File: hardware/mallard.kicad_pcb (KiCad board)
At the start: 4 copper layers, 101.6 x 101.6 mm, 81 parts, among them J1 USB_A, J2 Conn_02x03_Odd_Even, J3 Conn_01x03, J4 Conn_01x03, J5 Conn_01x03, J6 Conn_01x03, SW1 RESET Switch, U10 LTC1983ES6-3, U11 STM32L4Q5xx, U12 LTC3529EDCB, U4 BQ24210DQCT, U5 TMUX1309, U6 TMUX1309, U7 LMP7721, U8 TPS71710DRVR, U9 LMV554

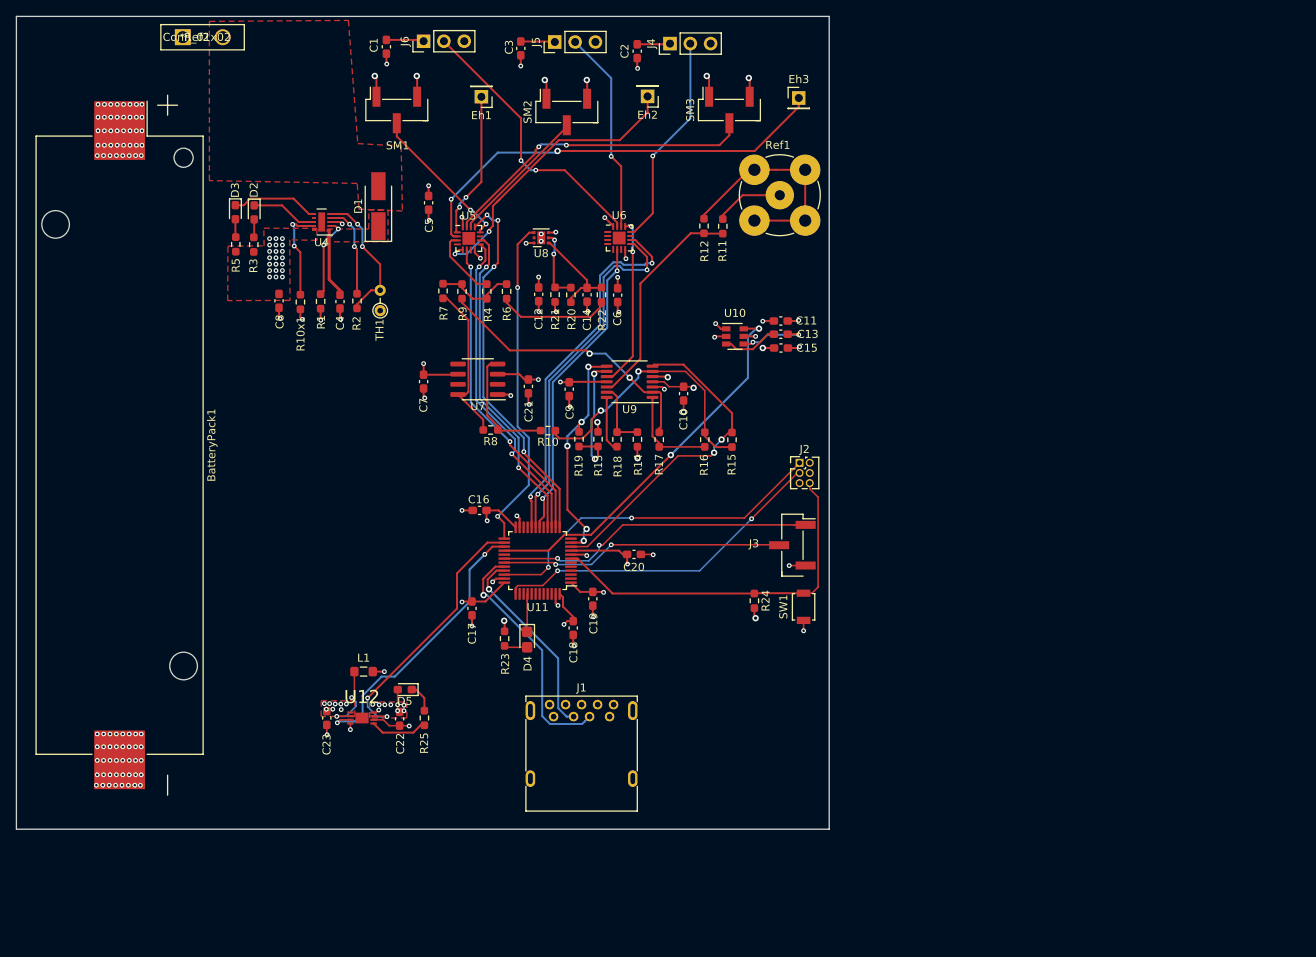
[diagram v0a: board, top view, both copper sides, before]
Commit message: Revised layout, fixed schematic errors
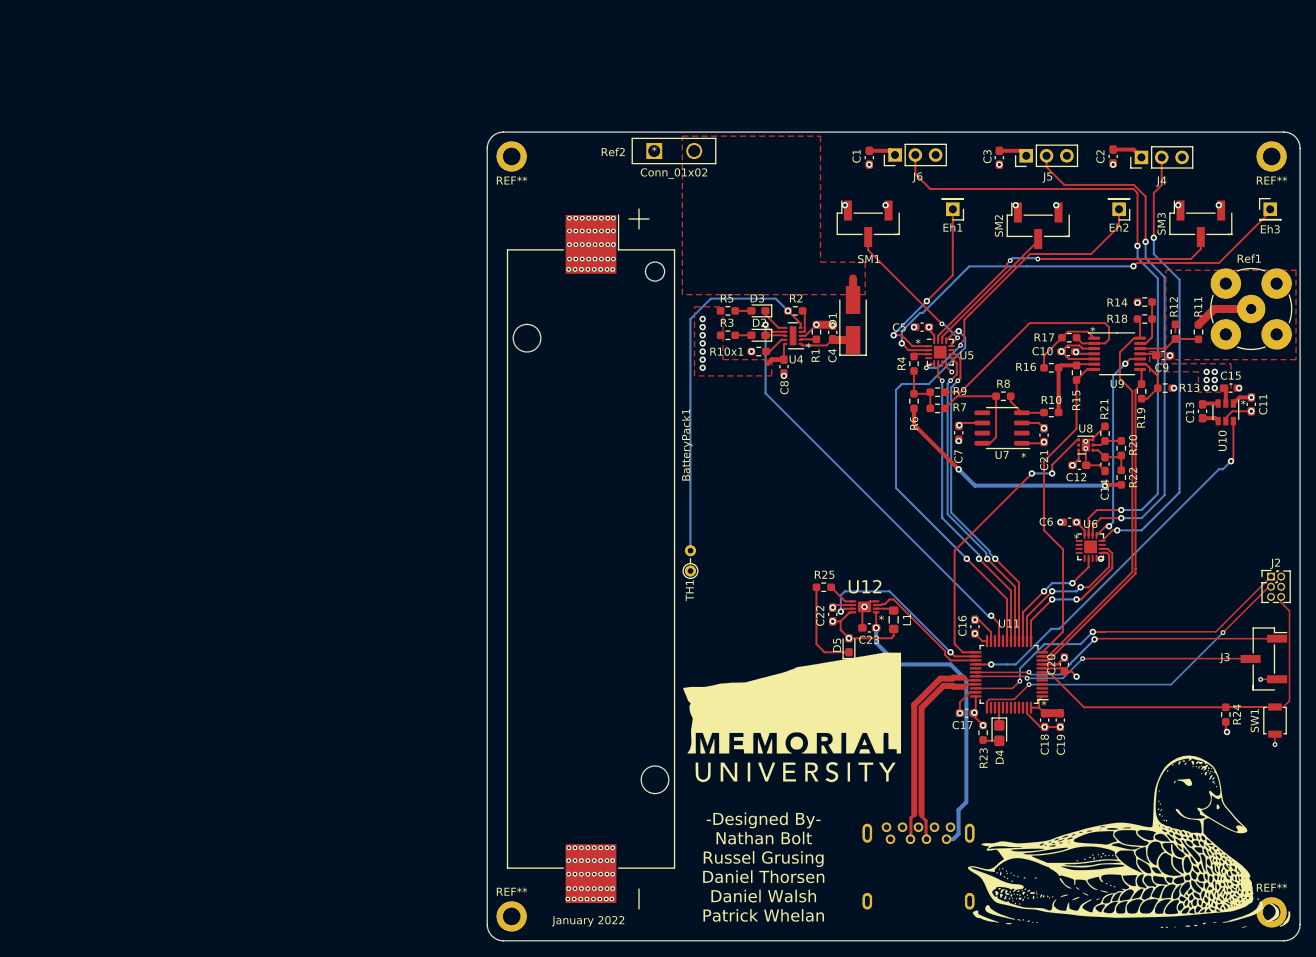
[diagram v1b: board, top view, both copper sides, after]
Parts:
- added G***: LOGO, hardware:mallardImage, F.Cu at (178.8, 136.7)
- added G***: LOGO, hardware:munLogo, F.Cu at (137.2, 121.4)
- added REF**: MountingHole_2.2mm_M2_DIN965_Pad, MountingHole:MountingHole_2.2mm_M2_DIN965_Pad, F.Cu at (197.1, 51.3)
- added REF**: MountingHole_2.2mm_M2_DIN965_Pad, MountingHole:MountingHole_2.2mm_M2_DIN965_Pad, F.Cu at (197.1, 145.8)
- added REF**: MountingHole_2.2mm_M2_DIN965_Pad, MountingHole:MountingHole_2.2mm_M2_DIN965_Pad, F.Cu at (102.1, 146.3)
- added REF**: MountingHole_2.2mm_M2_DIN965_Pad, MountingHole:MountingHole_2.2mm_M2_DIN965_Pad, F.Cu at (102.1, 51.3)
- J1: moved to B.Cu
- moved C9 74.4 mm to (183.5, 76.2), turned to 0 degrees
- moved U8 72.8 mm to (173.9, 87.4)
- moved R20 71.4 mm to (178.3, 87.8)
- moved R13 71.2 mm to (183.8, 80.3), turned to 180 degrees
- moved R21 70.9 mm to (176.3, 86.0), turned to 90 degrees
- moved C12 70.9 mm to (173.1, 89.9), turned to 0 degrees
- moved R19 70.6 mm to (180.8, 80.7)
- moved U6 70.4 mm to (174.5, 100.1)
- moved R22 68.9 mm to (178.3, 91.4)
- moved C23 68.7 mm to (146.8, 110.2), turned to 180 degrees
- moved C14 68.1 mm to (176.3, 89.8)
- moved R18 67.7 mm to (181.3, 71.6), turned to 0 degrees
- moved C7 67.2 mm to (158.0, 85.9)
- moved L1 66.6 mm to (149.9, 109.2), turned to 90 degrees
- moved D3 66.5 mm to (133.0, 70.6), turned to 180 degrees
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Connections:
- U11 pad 10: Eh_Sense -> Temp_Sense
- U11 pad 11: Temp_Sense -> Ref_Out
- U11 pad 12: Ref_Elec -> Eh_Sense
- U11 pad 13: Moisture_Sense -> MUX2_A1
- U11 pad 14: MUX1_EN -> MUX2_A0
- U11 pad 15: MUX1_A0 -> MUX2_EN
- U11 pad 17: Net-(U11-Pad17) -> MUX1_A0
- U11 pad 18: MUX2_EN -> MUX1_EN
- U11 pad 19: MUX2_A0 -> Moisture_Sense
- U11 pad 20: MUX2_A1 -> Net-(U11-Pad20)
- U12 pad 9: (no net) -> GND
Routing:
- net Charge_EN: track 0.00 -> 54.8 mm, vias 0 -> 2
- net Net-(J6-Pad2): track 34.6 -> 82.3 mm
- net Ref_Out: track 6.97 -> 49.5 mm
- net Net-(J5-Pad2): track 25.4 -> 65.4 mm, vias 1 -> 2
- net +5V: track 0.00 -> 38.4 mm, vias 8 -> 2
- net Net-(J4-Pad2): track 26.9 -> 55.8 mm, vias 1 -> 2
- net MUX2_A1: track 46.9 -> 18.8 mm
- net Net-(R2-Pad2): track 17.6 -> 45.6 mm, vias 2 -> 1
- net Net-(R12-Pad2): track 28.2 -> 1.16 mm
- net MUX2_A0: track 45.4 -> 18.8 mm
- net Net-(R10-Pad1): track 34.7 -> 10.2 mm, vias 2 -> 0
- net MUX2_EN: track 38.9 -> 15.2 mm
- net Net-(R11-Pad1): track 28.0 -> 7.83 mm
- net +3V3: track 80.3 -> 60.7 mm, vias 91 -> 63
- net 5V_SHDN_L: track 35.5 -> 16.1 mm, vias 2 -> 0
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- added copper zone on F.Cu, net -3V3
- added copper zone on F.Cu, net Net-(R12-Pad2)
- removed copper zone on F.Cu, net +5V
- removed copper zone on Power, net +5V
- removed copper zone on F.Cu, net Net-(C4-Pad1)
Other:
- board size 101.6 x 101.6 mm -> 101.6 x 101.1 mm
- board text added: "*"
- board text added: "-Designed By- Nathan Bolt Russel Grusing Daniel Thorsen Daniel Walsh Patrick Whelan"
- board text added: "January 2022"

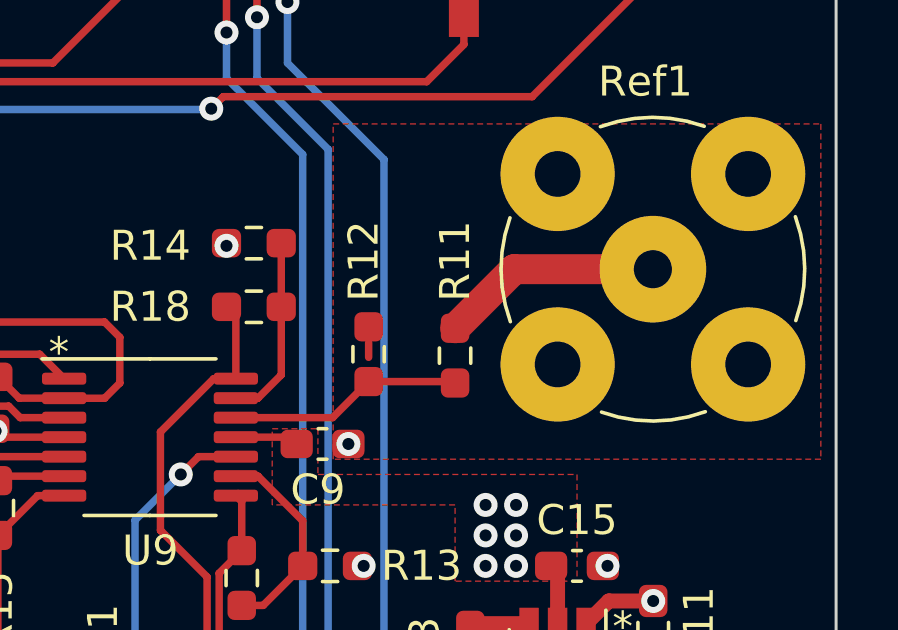
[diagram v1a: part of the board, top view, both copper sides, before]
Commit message: Changes some components on BOM
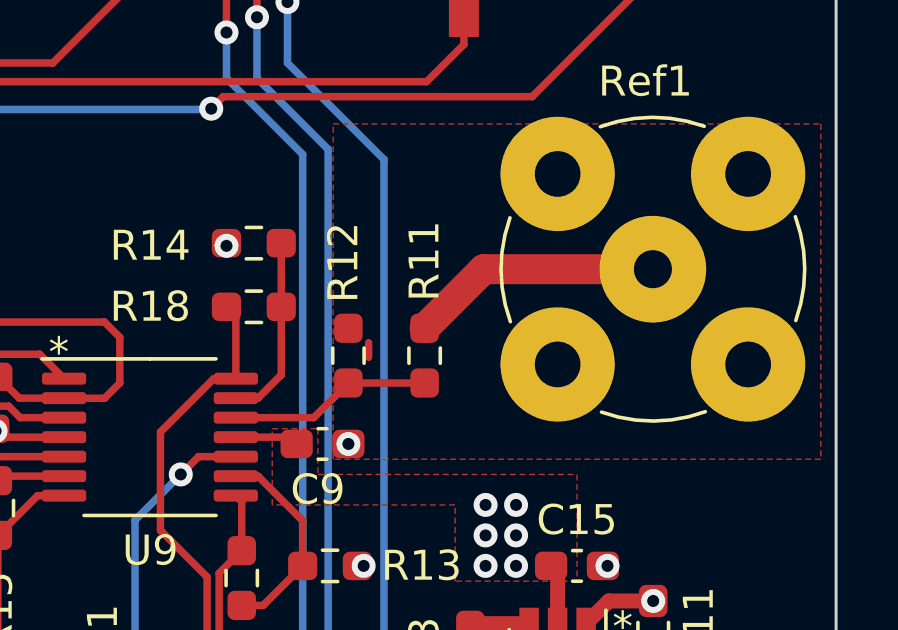
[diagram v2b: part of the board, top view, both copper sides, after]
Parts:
- moved R11 1.02 mm to (186.9, 73.3)
- moved R12 0.68 mm to (184.4, 73.3)
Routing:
- net Net-(R11-Pad1): track 7.83 -> 6.77 mm
- net Net-(R11-Pad2): track 7.41 -> 8.42 mm

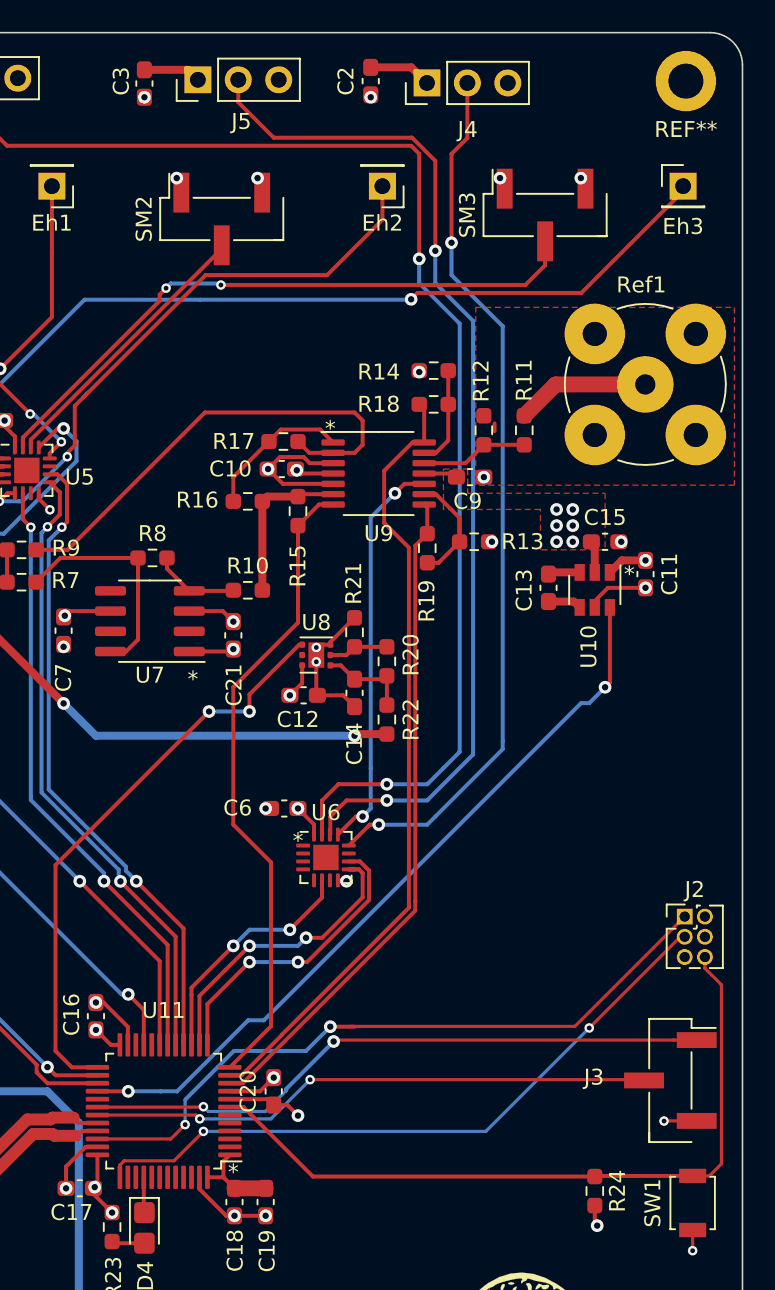
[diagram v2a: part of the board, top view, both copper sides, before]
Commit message: Replaced -3V charge pump with LM828
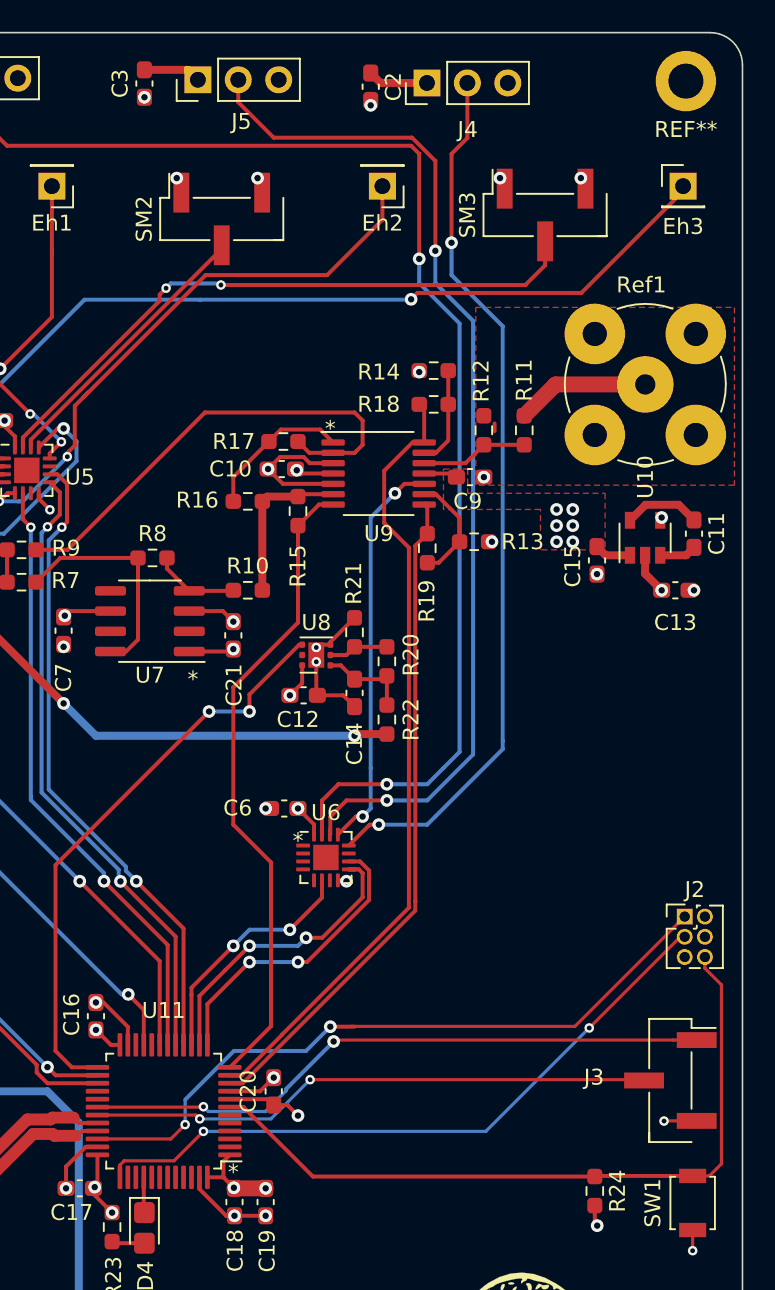
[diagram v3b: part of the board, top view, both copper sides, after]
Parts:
- C15: value 10uF -> 1uF
- U10: value LTC1983ES6-3 -> LM828; footprint Package_TO_SOT_SMD:SOT-23-6 -> Package_TO_SOT_SMD:SOT-23-5
- moved C13 7.98 mm to (196.4, 83.3), turned to 0 degrees
- moved U10 4.55 mm to (194.5, 80.0), turned to 90 degrees
- moved C11 3.97 mm to (197.6, 79.8)
- moved C15 1.28 mm to (191.5, 81.4), turned to 270 degrees
- moved C2 0.35 mm to (177.3, 51.7)
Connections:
- C11 pad 1: +3V3 -> Net-(C11-Pad1)
- C11 pad 2: GND -> Net-(C11-Pad2)
- C13 pad 1: Net-(C13-Pad1) -> +3V3
- C13 pad 2: Net-(C13-Pad2) -> GND
- U10 pad 1: +3V3 -> -3V3
- U10 pad 2: -3V3 -> +3V3
- U10 pad 3: Net-(C13-Pad1) -> Net-(C11-Pad2)
- U10 pad 4: Net-(C13-Pad2) -> GND
- U10 pad 5: GND -> Net-(C11-Pad1)
- U11 pad 28: -3V3_SHDN_L -> Net-(U11-Pad28)
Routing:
- net -3V3_SHDN_L: track 47.6 -> 0.00 mm, vias 2 -> 0
- net Net-(C11-Pad1): track 0.00 -> 4.82 mm
- net GND: track 58.8 -> 55.4 mm, vias 73 -> 74
- net Net-(C11-Pad2): track 0.00 -> 2.33 mm
- net Net-(C13-Pad2): track 2.11 -> 0.00 mm
- net Net-(C13-Pad1): track 2.00 -> 0.00 mm
- net +3V3: track 60.7 -> 60.6 mm, vias 63 -> 65
